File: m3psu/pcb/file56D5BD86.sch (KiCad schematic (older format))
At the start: 44 parts

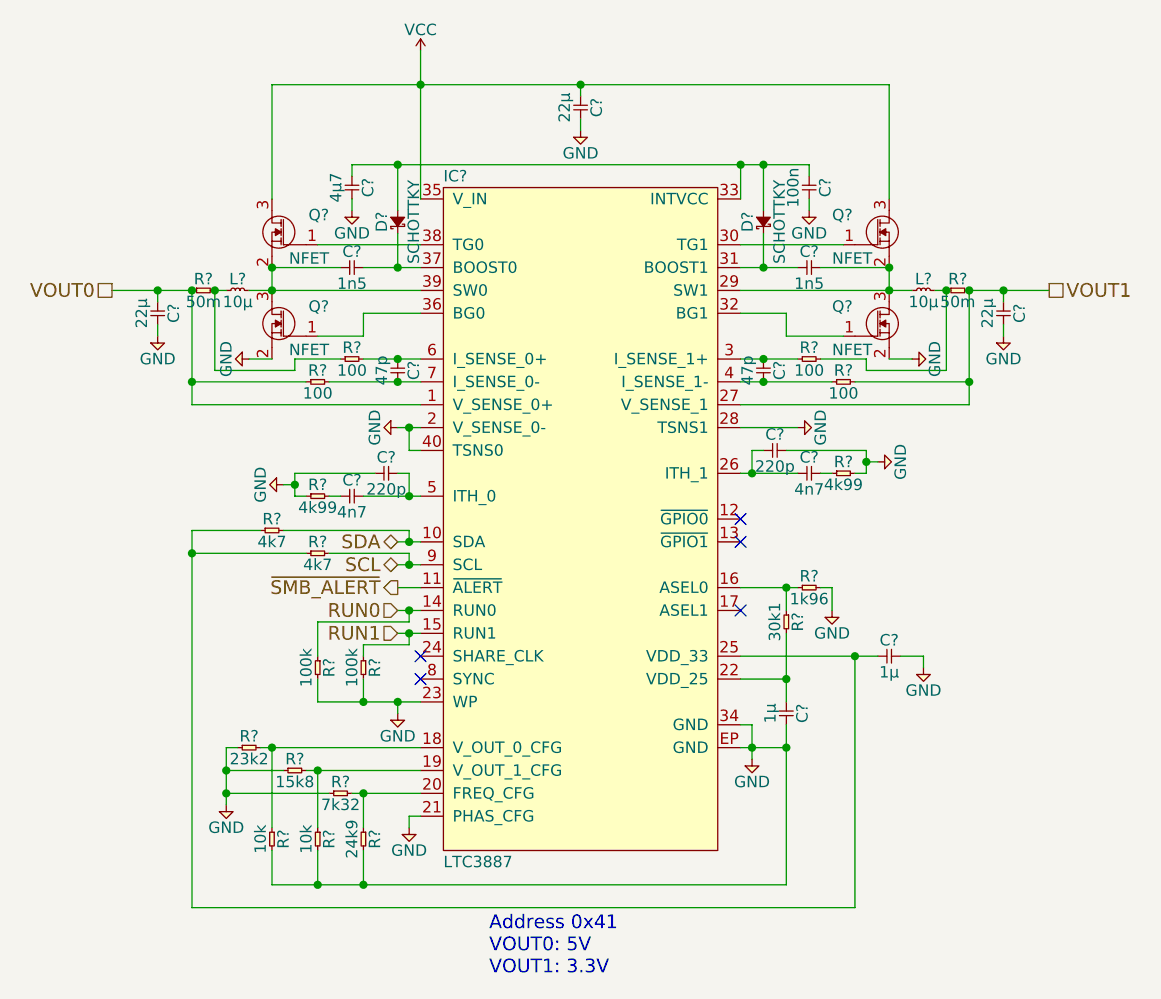
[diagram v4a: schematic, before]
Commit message: Add farnell numbers and footprints to dc converter parts
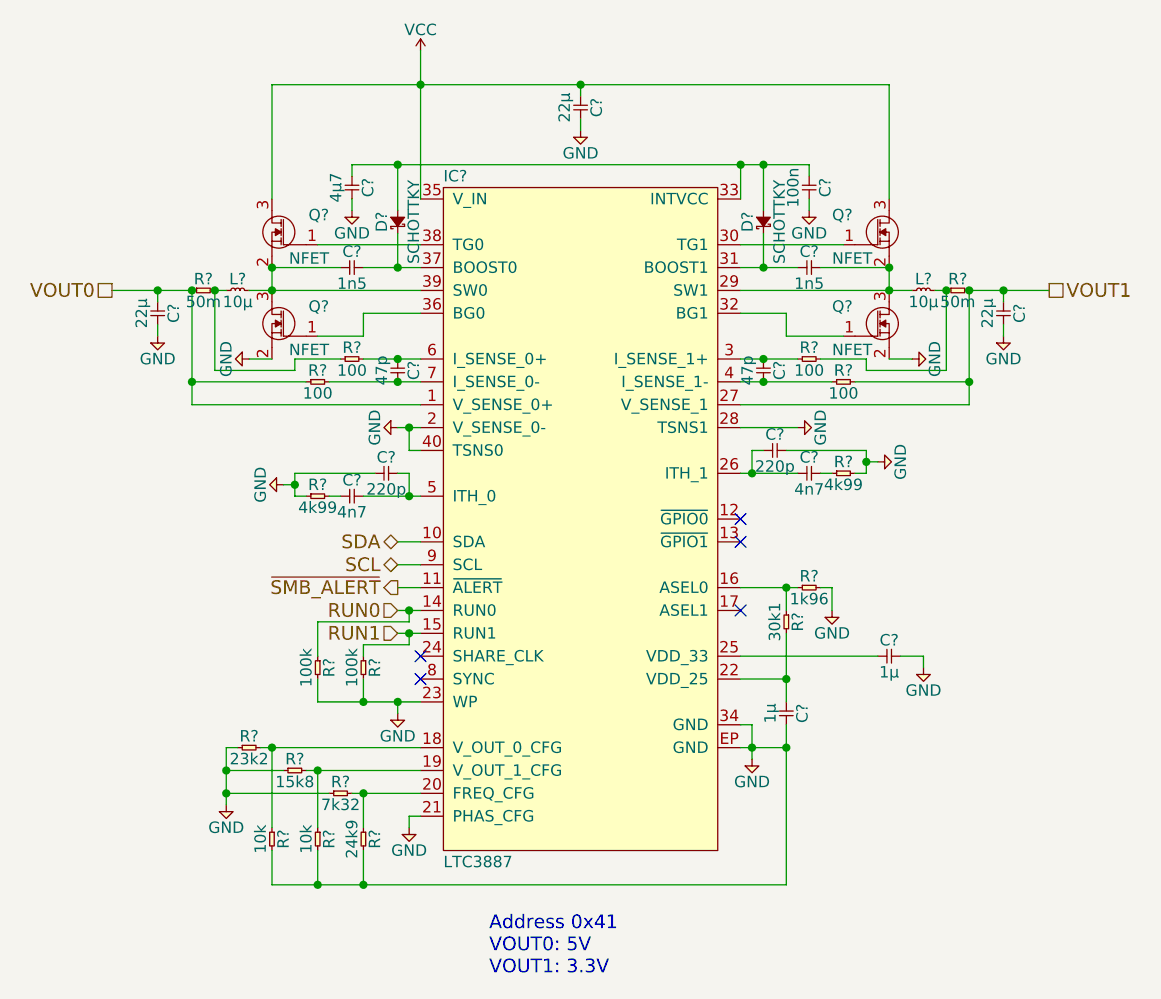
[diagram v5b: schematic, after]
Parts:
- removed R? (x2): 4k7, symbol R
- C? (x2): footprint (none) -> agg:0402; Farnell (none) -> 2210833
- C?: Farnell (none) -> 2426959
- C? (x3), R? (x2): footprint (none) -> agg:0603
- C? (x2): footprint (none) -> agg:0402; Farnell (none) -> 2210781
- C? (x2): footprint (none) -> agg:0402; Farnell (none) -> 2218855
- C?: footprint (none) -> agg:0402; Farnell (none) -> 2496811
- C? (x2): footprint (none) -> agg:0402; Farnell (none) -> 2496786
- C? (x2): footprint (none) -> agg:0402; Farnell (none) -> 2210772
- D? (x2): footprint (none) -> agg:0603-LED
- L? (x2): footprint (none) -> agg:TYS5040
- R? (x4): footprint (none) -> agg:0402; Farnell (none) -> 2447095
- R?: footprint (none) -> agg:0402; Farnell (none) -> 1803690
- R? (x2): footprint (none) -> agg:0402; Farnell (none) -> 2447096
- R?: footprint (none) -> agg:0402; Farnell (none) -> 2302774
- R?: footprint (none) -> agg:0402; Farnell (none) -> 2302757
- R?: footprint (none) -> agg:0402; Farnell (none) -> 2073231
- R?: footprint (none) -> agg:0402; Farnell (none) -> 1803065
- R?: footprint (none) -> agg:0402; Farnell (none) -> 2072900
- R? (x2): footprint (none) -> agg:0402; Farnell (none) -> 1469715
- R? (x2): footprint (none) -> agg:0402; Farnell (none) -> 2447094

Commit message: Added current monitor and control for pyros. Modified DC/DC converters.
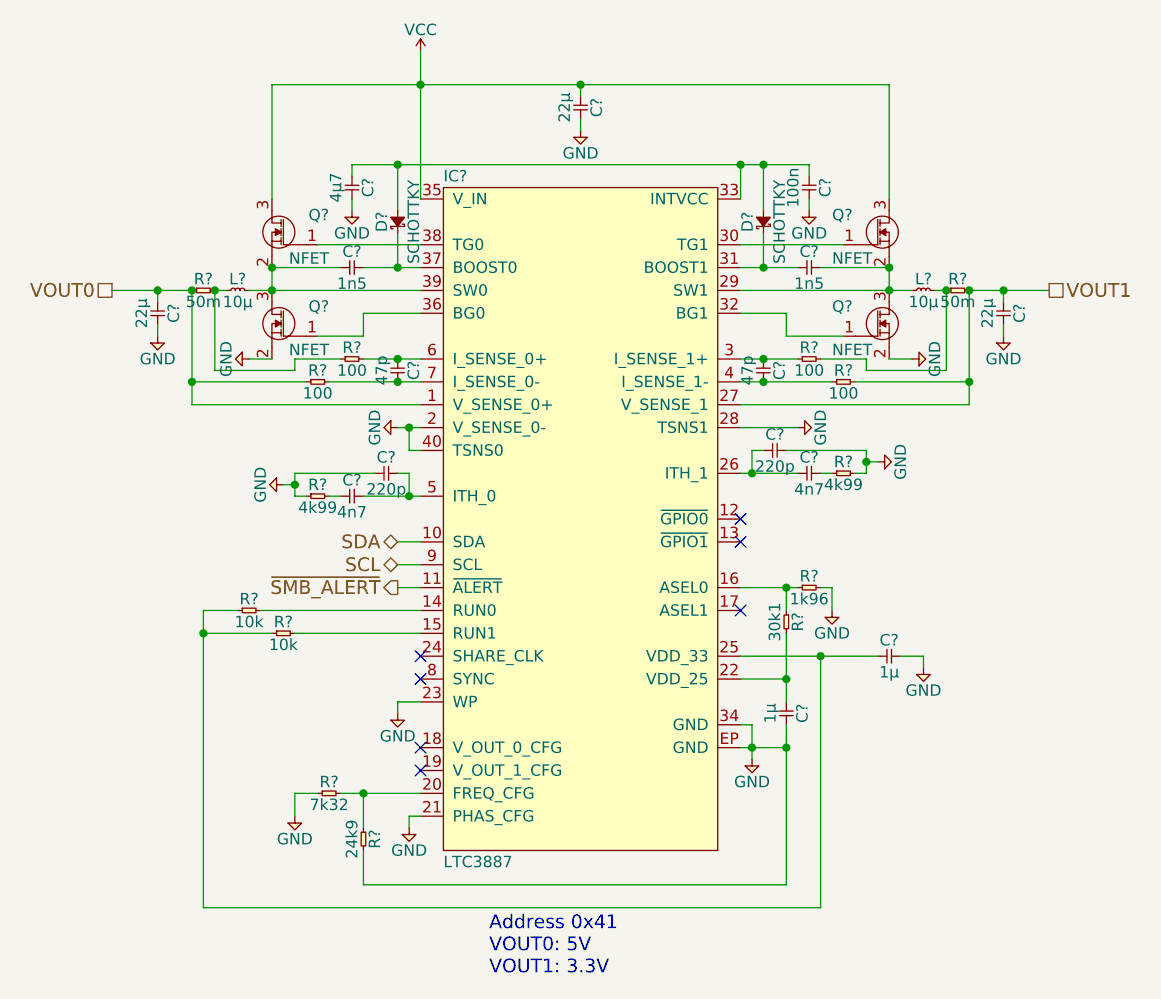
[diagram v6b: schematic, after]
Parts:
- removed R? (x2): 10k, agg:0402, symbol R
- removed R?: 23k2, agg:0402, symbol R
- removed R?: 15k8, agg:0402, symbol R
- removed R? (x2): 100k, agg:0402, symbol R
- added R? (x2): 10k, agg:0402, symbol R
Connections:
- net at C?.1, IC?.25 (VDD_33): now also R?.1, R?.1
- net RUN0: no longer names the net of IC?.14 (RUN0)
- net RUN0: now also R?.2
- net RUN1: no longer names the net of IC?.15 (RUN1)
- net RUN1: now also R?.2
- no-connect marks 5 -> 7
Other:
- moved on the sheet: R?
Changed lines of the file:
@@
 $Descr A4 11693 8268
 encoding utf-8
-Sheet 5 10
+Sheet 5 12
 Title ""
 Date ""
@@
 $EndComp
 $Comp
-L R R?
-U 1 1 56D5F63E
-P 4700 5250
-F 0 "R?" H 4750 5300 50  0000 C CNN
-F 1 "10k" H 4750 5200 50  0000 C CNN
-F 2 "agg:0402" H 4700 5250 50  0001 C CNN
-F 3 "" H 4700 5250 50  0001 C CNN
-F 4 "2447096" H 4700 5250 60  0001 C CNN "Farnell"
-	1    4700 5250
-	0    1    1    0
-$EndComp
-$Comp
-L R R?
-U 1 1 56D5F645
-P 4500 5250
-F 0 "R?" H 4550 5300 50  0000 C CNN
-F 1 "10k" H 4550 5200 50  0000 C CNN
-F 2 "agg:0402" H 4500 5250 50  0001 C CNN
-F 3 "" H 4500 5250 50  0001 C CNN
-F 4 "2447096" H 4500 5250 60  0001 C CNN "Farnell"
-	1    4500 5250
-	0    1    1    0
-$EndComp
-$Comp
-L R R?
-U 1 1 56D5F64C
-P 4350 4900
-F 0 "R?" H 4400 4950 50  0000 C CNN
-F 1 "23k2" H 4400 4850 50  0000 C CNN
-F 2 "agg:0402" H 4350 4900 50  0001 C CNN
-F 3 "" H 4350 4900 50  0001 C CNN
-F 4 "2302774" H 4350 4900 60  0001 C CNN "Farnell"
-	1    4350 4900
-	1    0    0    -1
-$EndComp
-$Comp
-L R R?
-U 1 1 56D5F653
-P 4550 5000
-F 0 "R?" H 4600 5050 50  0000 C CNN
-F 1 "15k8" H 4600 4950 50  0000 C CNN
-F 2 "agg:0402" H 4550 5000 50  0001 C CNN
-F 3 "" H 4550 5000 50  0001 C CNN
-F 4 "2302757" H 4550 5000 60  0001 C CNN "Farnell"
-	1    4550 5000
-	1    0    0    -1
-$EndComp
-$Comp
-L R R?
-U 1 1 56D5F65A
-P 4750 5100
-F 0 "R?" H 4800 5150 50  0000 C CNN
-F 1 "7k32" H 4800 5050 50  0000 C CNN
-F 2 "agg:0402" H 4750 5100 50  0001 C CNN
-F 3 "" H 4750 5100 50  0001 C CNN
-F 4 "2073231" H 4750 5100 60  0001 C CNN "Farnell"
-	1    4750 5100
-	1    0    0    -1
-$EndComp
-$Comp
 L GND #PWR054
 U 1 1 56D5F661
-P 4300 5150
-F 0 "#PWR054" H 4170 5190 50  0001 L CNN
-F 1 "GND" H 4300 5050 50  0000 C CNN
-F 2 "" H 4300 5150 60  0000 C CNN
-F 3 "" H 4300 5150 60  0000 C CNN
-	1    4300 5150
+P 4600 5200
+F 0 "#PWR054" H 4470 5240 50  0001 L CNN
+F 1 "GND" H 4600 5100 50  0000 C CNN
+F 2 "" H 4600 5200 60  0000 C CNN
+F 3 "" H 4600 5200 60  0000 C CNN
+	1    4600 5200
 	1    0    0    -1
 $EndComp
@@
 Text HLabel 5050 4100 0    60   BiDi ~ 0
 SCL
-Text HLabel 5050 4300 0    60   Input ~ 0
-RUN0
-Text HLabel 5050 4400 0    60   Input ~ 0
-RUN1
 $Comp
 L GND #PWR055
@@
 	5050 3700 5100 3700
 Wire Wire Line
-	5100 4450 5100 4400
-Wire Wire Line
 	7100 3600 6750 3600
 Connection ~ 7100 3650
@@
 Wire Wire Line
 	6550 3700 6800 3700
-Connection ~ 5100 4400
-Connection ~ 5100 4300
-Wire Wire Line
-	5100 4350 5100 4300
 Wire Wire Line
 	5050 4100 5150 4100
 Wire Wire Line
 	5050 4000 5150 4000
-Wire Wire Line
-	5050 4300 5150 4300
-Wire Wire Line
-	5050 4400 5150 4400
 Wire Wire Line
 	6900 4200 6950 4200
@@
 	5050 4700 5050 4750
 Wire Wire Line
-	4700 4700 5150 4700
-Connection ~ 4300 5100
-Wire Wire Line
-	4300 5100 4750 5100
-Connection ~ 4300 5000
-Wire Wire Line
-	4550 5000 4300 5000
-Wire Wire Line
-	4300 4900 4300 5150
-Wire Wire Line
-	4350 4900 4300 4900
+	5050 4700 5150 4700
 Connection ~ 4900 5100
-Connection ~ 4700 5000
-Connection ~ 4500 4900
-Wire Wire Line
-	4450 4900 5150 4900
-Wire Wire Line
-	4500 5250 4500 4900
-Wire Wire Line
-	4650 5000 5150 5000
-Wire Wire Line
-	4700 5250 4700 5000
-Wire Wire Line
-	4850 5100 5150 5100
+Wire Wire Line
+	4800 5100 5150 5100
 Wire Wire Line
 	4900 5100 4900 5250
 Wire Wire Line
 	5100 5200 5150 5200
-Connection ~ 4900 5500
 Wire Wire Line
 	4900 5350 4900 5500
-Connection ~ 4700 5500
-Wire Wire Line
-	4700 5350 4700 5500
-Wire Wire Line
-	4500 5500 4500 5350
 Connection ~ 6750 4900
-Wire Wire Line
-	6750 5500 4500 5500
 Wire Wire Line
 	7250 4500 7350 4500
@@
 $Comp
 L R R?
-U 1 1 56D5F7B5
-P 4900 4500
-F 0 "R?" H 4950 4550 50  0000 C CNN
-F 1 "100k" H 4950 4450 50  0000 C CNN
-F 2 "agg:0402" H 4900 4500 50  0001 C CNN
-F 3 "" H 4900 4500 50  0001 C CNN
-F 4 "2447094" H 4900 4500 60  0001 C CNN "Farnell"
-	1    4900 4500
-	0    1    1    0
-$EndComp
-Wire Wire Line
-	4900 4700 4900 4600
-Connection ~ 5050 4700
-Wire Wire Line
-	5100 4450 4900 4450
-Wire Wire Line
-	4900 4450 4900 4500
-Wire Wire Line
-	5100 4350 4700 4350
-Wire Wire Line
-	4700 4350 4700 4500
-$Comp
-L R R?
-U 1 1 56D5F7C2
-P 4700 4500
-F 0 "R?" H 4750 4550 50  0000 C CNN
-F 1 "100k" H 4750 4450 50  0000 C CNN
-F 2 "agg:0402" H 4700 4500 50  0001 C CNN
-F 3 "" H 4700 4500 50  0001 C CNN
-F 4 "2447094" H 4700 4500 60  0001 C CNN "Farnell"
-	1    4700 4500
-	0    1    1    0
-$EndComp
-Wire Wire Line
-	4700 4600 4700 4700
-Connection ~ 4900 4700
+U 1 1 56D5F65A
+P 4700 5100
+F 0 "R?" H 4750 5150 50  0000 C CNN
+F 1 "7k32" H 4750 5050 50  0000 C CNN
+F 2 "agg:0402" H 4700 5100 50  0001 C CNN
+F 3 "" H 4700 5100 50  0001 C CNN
+F 4 "2073231" H 4700 5100 60  0001 C CNN "Farnell"
+	1    4700 5100
+	1    0    0    -1
+$EndComp
+Wire Wire Line
+	4700 5100 4600 5100
+Wire Wire Line
+	4600 5100 4600 5200
+Wire Wire Line
+	6750 5500 4900 5500
+Wire Wire Line
+	6900 5600 6900 4500
+Wire Wire Line
+	4200 5600 6900 5600
+Connection ~ 6900 4500
+NoConn ~ 5150 4900
+NoConn ~ 5150 5000
+Wire Wire Line
+	4200 4300 4200 5600
+$Comp
+L R R?
+U 1 1 56DDBA26
+P 4350 4300
+F 0 "R?" H 4400 4350 50  0000 C CNN
+F 1 "10k" H 4400 4250 50  0000 C CNN
+F 2 "agg:0402" H 4350 4300 50  0001 C CNN
+F 3 "" H 4350 4300 50  0001 C CNN
+F 4 "2447096" H 4350 4300 60  0001 C CNN "Farnell"
+	1    4350 4300
+	1    0    0    -1
+$EndComp
+$Comp
+L R R?
+U 1 1 56DDBA2E
+P 4500 4400
+F 0 "R?" H 4550 4450 50  0000 C CNN
+F 1 "10k" H 4550 4350 50  0000 C CNN
+F 2 "agg:0402" H 4500 4400 50  0001 C CNN
+F 3 "" H 4500 4400 50  0001 C CNN
+F 4 "2447096" H 4500 4400 60  0001 C CNN "Farnell"
+	1    4500 4400
+	1    0    0    -1
+$EndComp
+Wire Wire Line
+	4200 4300 4350 4300
+Wire Wire Line
+	4500 4400 4200 4400
+Connection ~ 4200 4400
+Wire Wire Line
+	4450 4300 5150 4300
+Wire Wire Line
+	4600 4400 5150 4400
 $EndSCHEMATC
